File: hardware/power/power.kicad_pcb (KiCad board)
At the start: 2 copper layers, 125 x 120 mm, 74 parts, among them J1 Jack-DC, J2 BATT, J3 Conn_01x05_Male, J4 RJ45, J5 RJ45, Q1 BSS123, Q2 PMOS, Q3 PMOS, Q4 BSS123, SW1 reset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

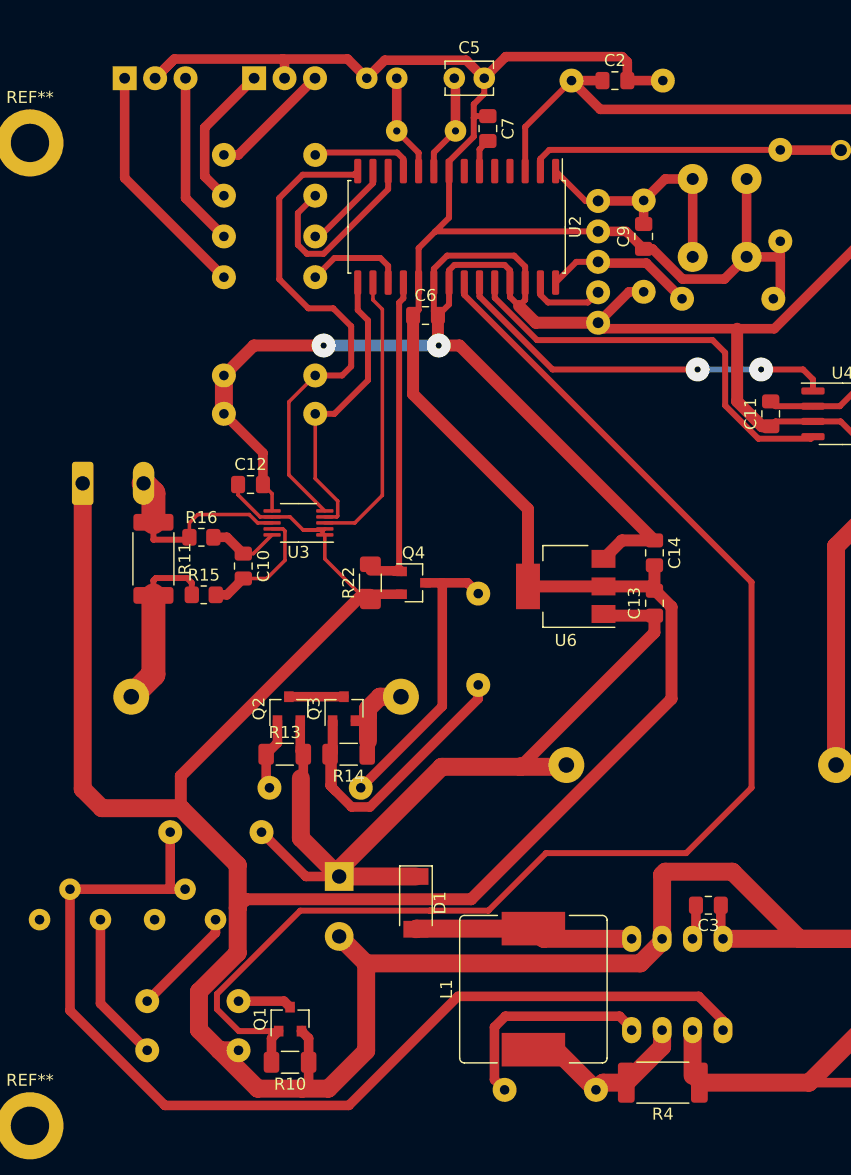
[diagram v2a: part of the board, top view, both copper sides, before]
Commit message: Convert power and vetus to new kicad format
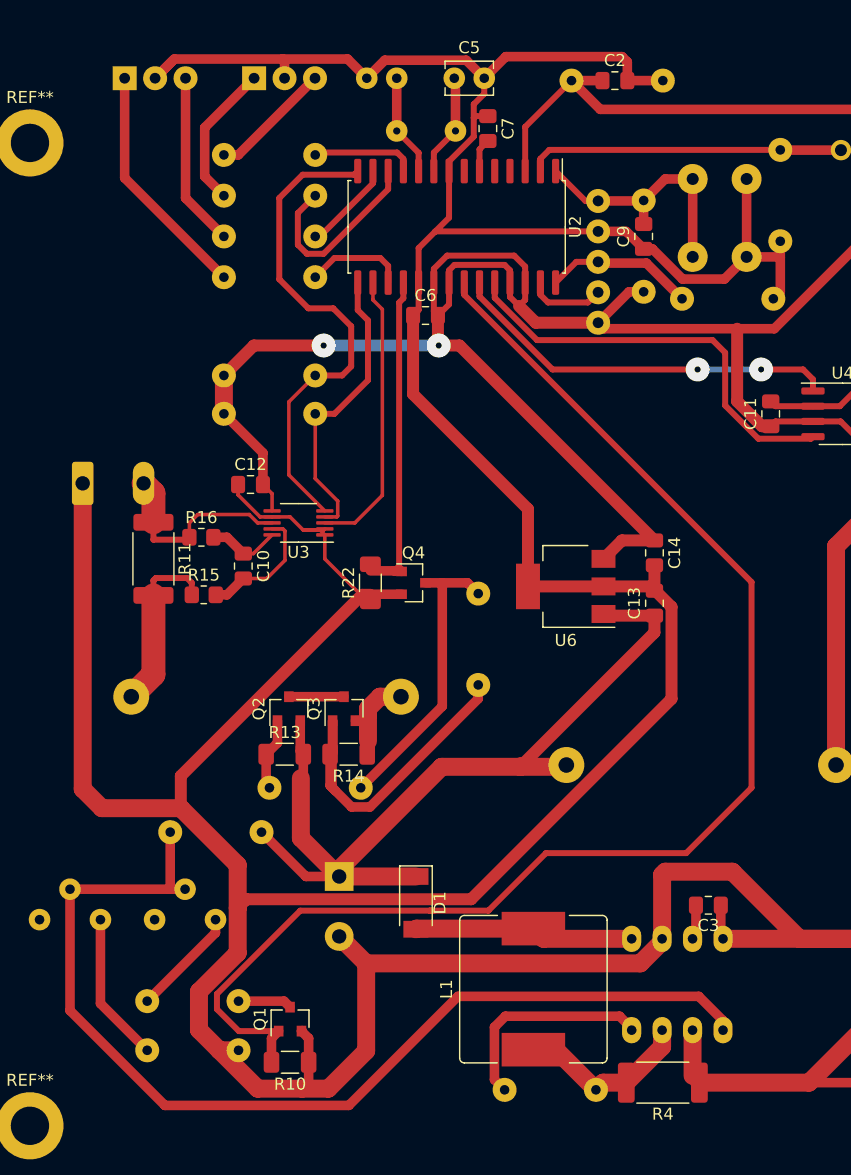
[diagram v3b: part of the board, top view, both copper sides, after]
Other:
- net class Default removed
